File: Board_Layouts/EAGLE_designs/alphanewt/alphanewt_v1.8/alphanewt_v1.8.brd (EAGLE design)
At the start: 158.4 x 117.7 mm, 98 parts, among them IC1 LM386N-1, Q1 TIP41C, Q2 TIP41C, Q3 TIP41C, Q4 TIP41C, Q5 TIP41C, Q6 TIP41C, Q7 TIP41C, T1 2N3904, T2 2N3904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

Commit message: Major update to alphanewt 1.8. Almost done routing the logic board.
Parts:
- moved X3 4.67 mm to (2.85, 35.1)
- moved U$2 0.95 mm to (134.3, 17.8)
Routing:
- net +5V: track 0.00 -> 242.6 mm, vias 0 -> 1
- net +3.3V: track 0.00 -> 222.2 mm, vias 0 -> 1
- net CAMERA_PWR: track 0.00 -> 211.1 mm, vias 0 -> 1
- net SDA: track 0.00 -> 187.8 mm
- net SCL: track 0.00 -> 172.2 mm
- net TEMP_EXT_2: track 0.00 -> 162.3 mm
- net BATT_EXT_PWR: track 0.00 -> 144.0 mm, vias 0 -> 2
- net VIN: track 0.00 -> 129.1 mm
- net TEMP_EXT_1: track 0.00 -> 124.1 mm, vias 0 -> 2
- net HEATER_CONTROL_2: track 0.00 -> 123.5 mm
- net HEATER_CONTROL_1: track 0.00 -> 122.4 mm
- net SPARE_1_PWR_RTN: track 0.00 -> 120.4 mm
- net RESET: track 0.00 -> 118.6 mm, vias 0 -> 3
- net S/A_PWR_IN: track 0.00 -> 114.7 mm
- net C_ID3: track 0.00 -> 103.5 mm
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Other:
- board text added: "GYRO + MPPT Hole"
- board text added: "STRUCT Mount"
- board text removed: "BATT1 HOLE"
- board text removed: "GYRO"

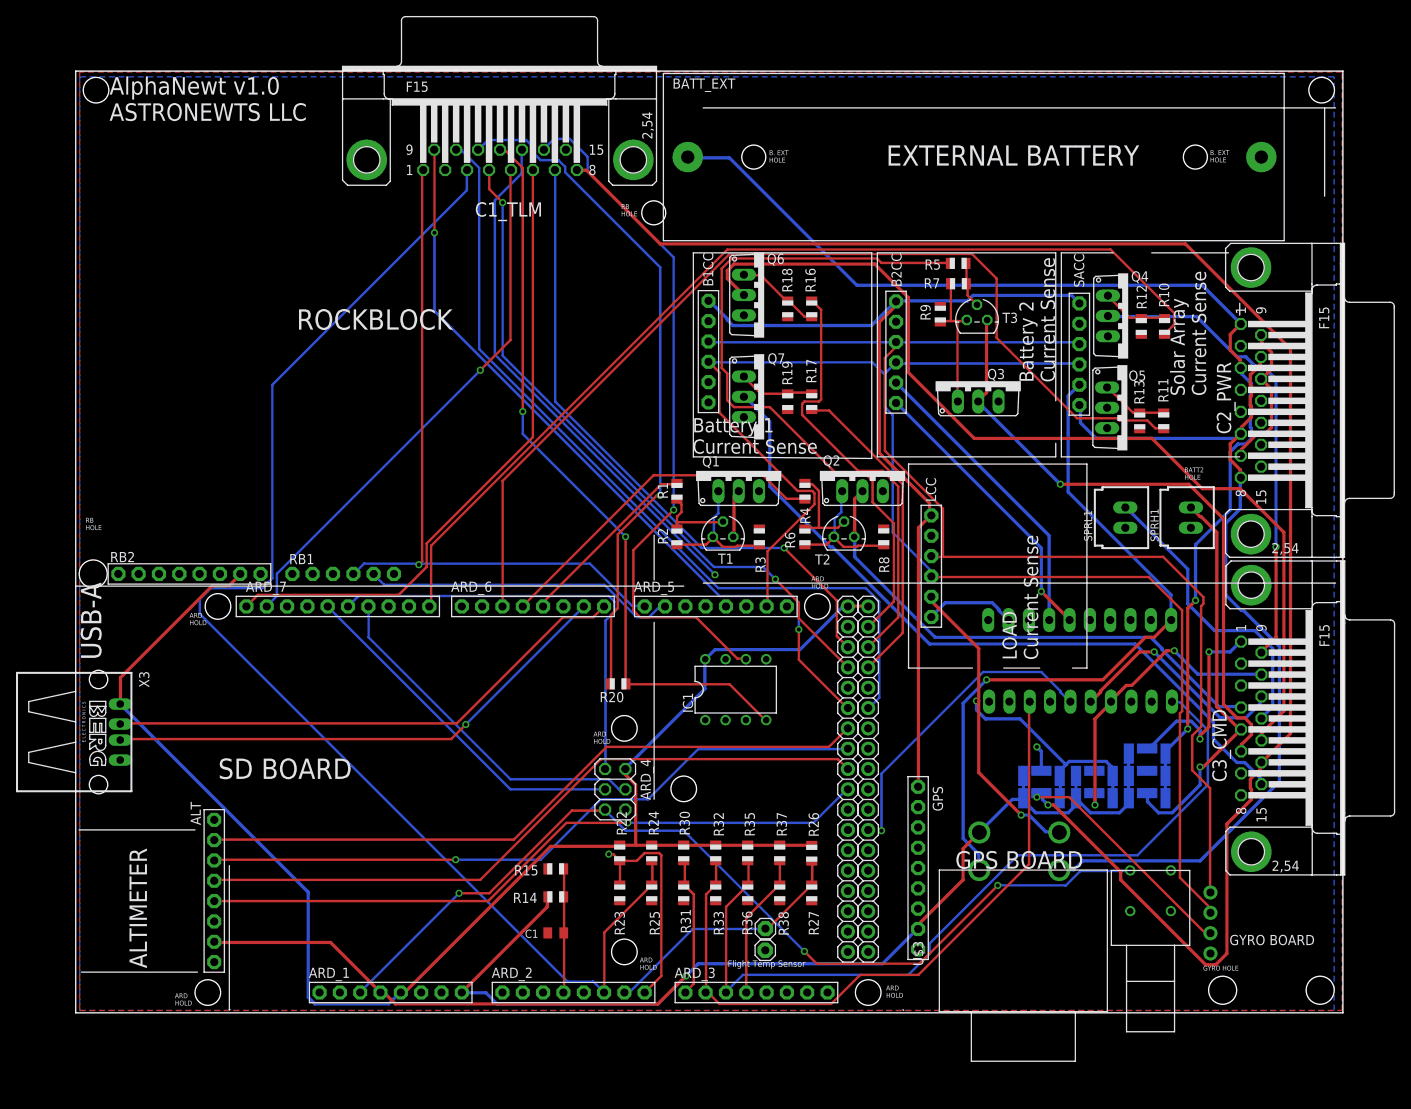
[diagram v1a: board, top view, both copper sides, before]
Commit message: Final updates to AlphaNewt v1.8 for review (fully routed)
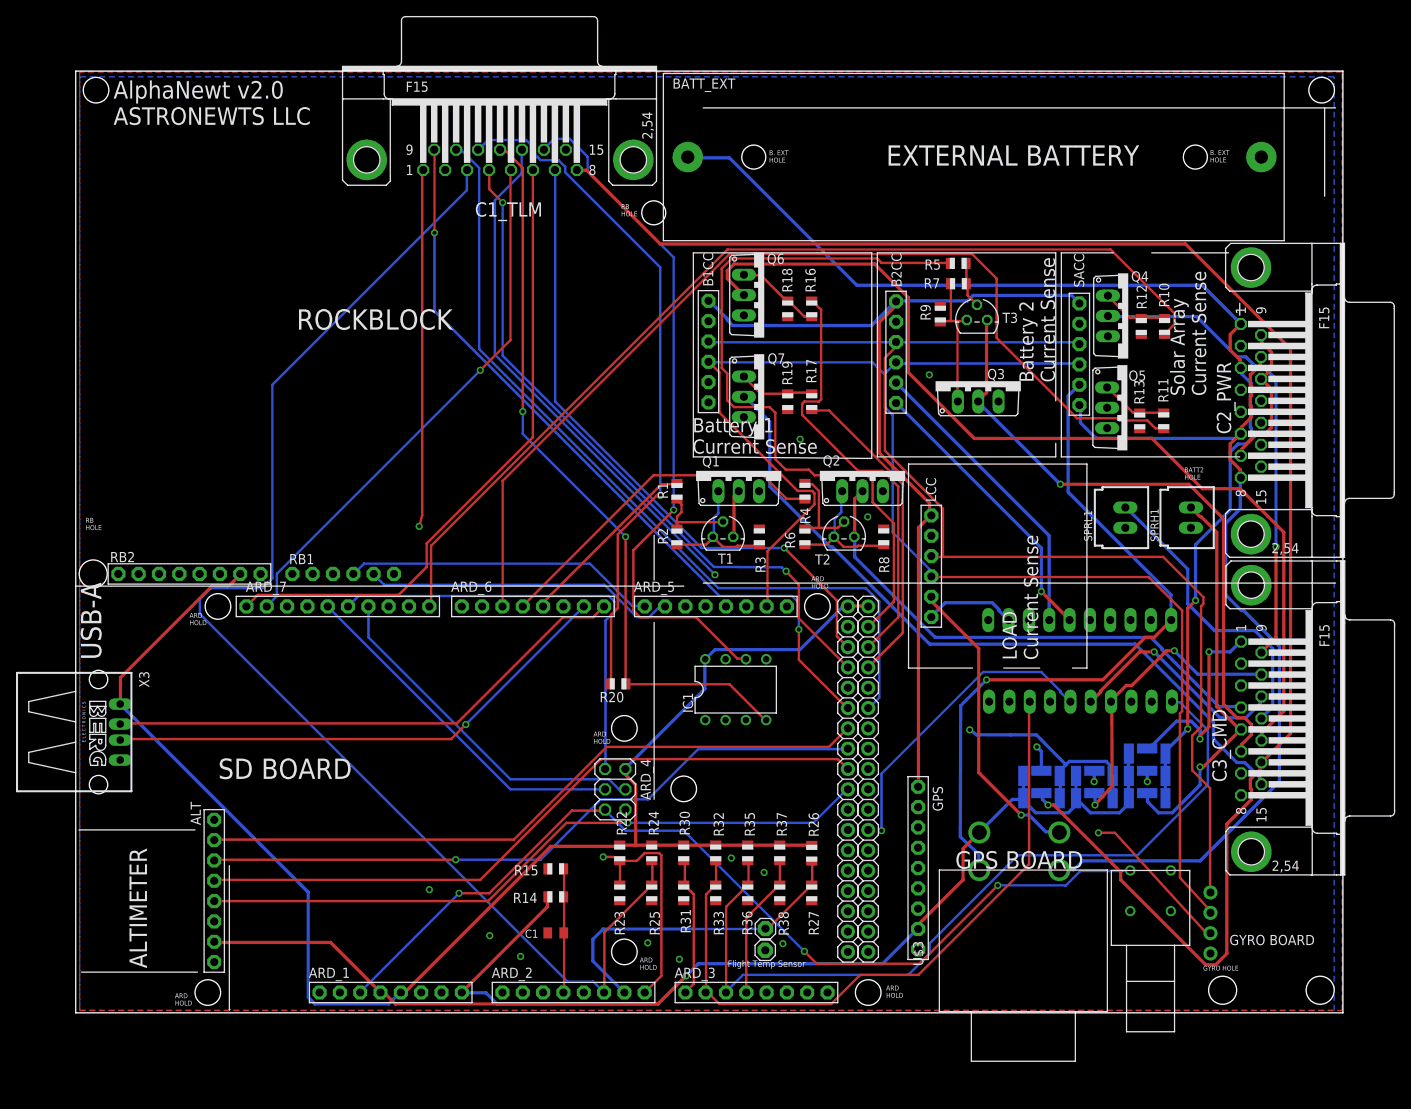
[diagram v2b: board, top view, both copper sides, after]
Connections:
- removed net BATT2_TS2: X1.3
- removed net GPS_RX: GPS.6
- removed net GPS_TX: GPS.5
- removed net S/A_PWR_OUT_RTN: X2.2
- net BATT_2_TS2: now also X1.3
- net RX1: now also GPS.5
- net S/A_PWR_RTN: now also X2.2
- net TX1: now also GPS.6
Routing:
- net BATT_2_TS2: track 18.2 -> 95.3 mm
- net TX1: track 0.00 -> 64.2 mm
- net RX1: track 0.00 -> 55.1 mm
- net GND: track 0.00 -> 48.5 mm, vias 0 -> 11
- net PYRO_2_PWR: track 0.00 -> 40.3 mm, vias 0 -> 1
- net S/A_PWR_RTN: track 18.9 -> 44.1 mm
- net FLT_CMP_TEMP: track 32.1 -> 41.5 mm
- net GYRO_PWR: track 58.1 -> 65.3 mm
- net SPARE_HIGH_1_CONTROL: track 89.1 -> 92.5 mm
- net PYRO_1_PWR_RTN: track 76.5 -> 79.3 mm
- net C_ID1: track 84.4 -> 85.7 mm
- net HEATER_1_PWR: track 35.3 -> 36.3 mm, vias 0 -> 1
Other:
- board text added: "AlphaNewt v2.0 ASTRONEWTS LLC"
- board text removed: "AlphaNewt v1.0 ASTRONEWTS LLC"
